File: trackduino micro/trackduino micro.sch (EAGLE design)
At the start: 28 parts, among them IC2 74AHC1G125DBV, SW1 SPST_TACT-KMR2, U1 ATMEGA168MLF, Y1 16MHZ

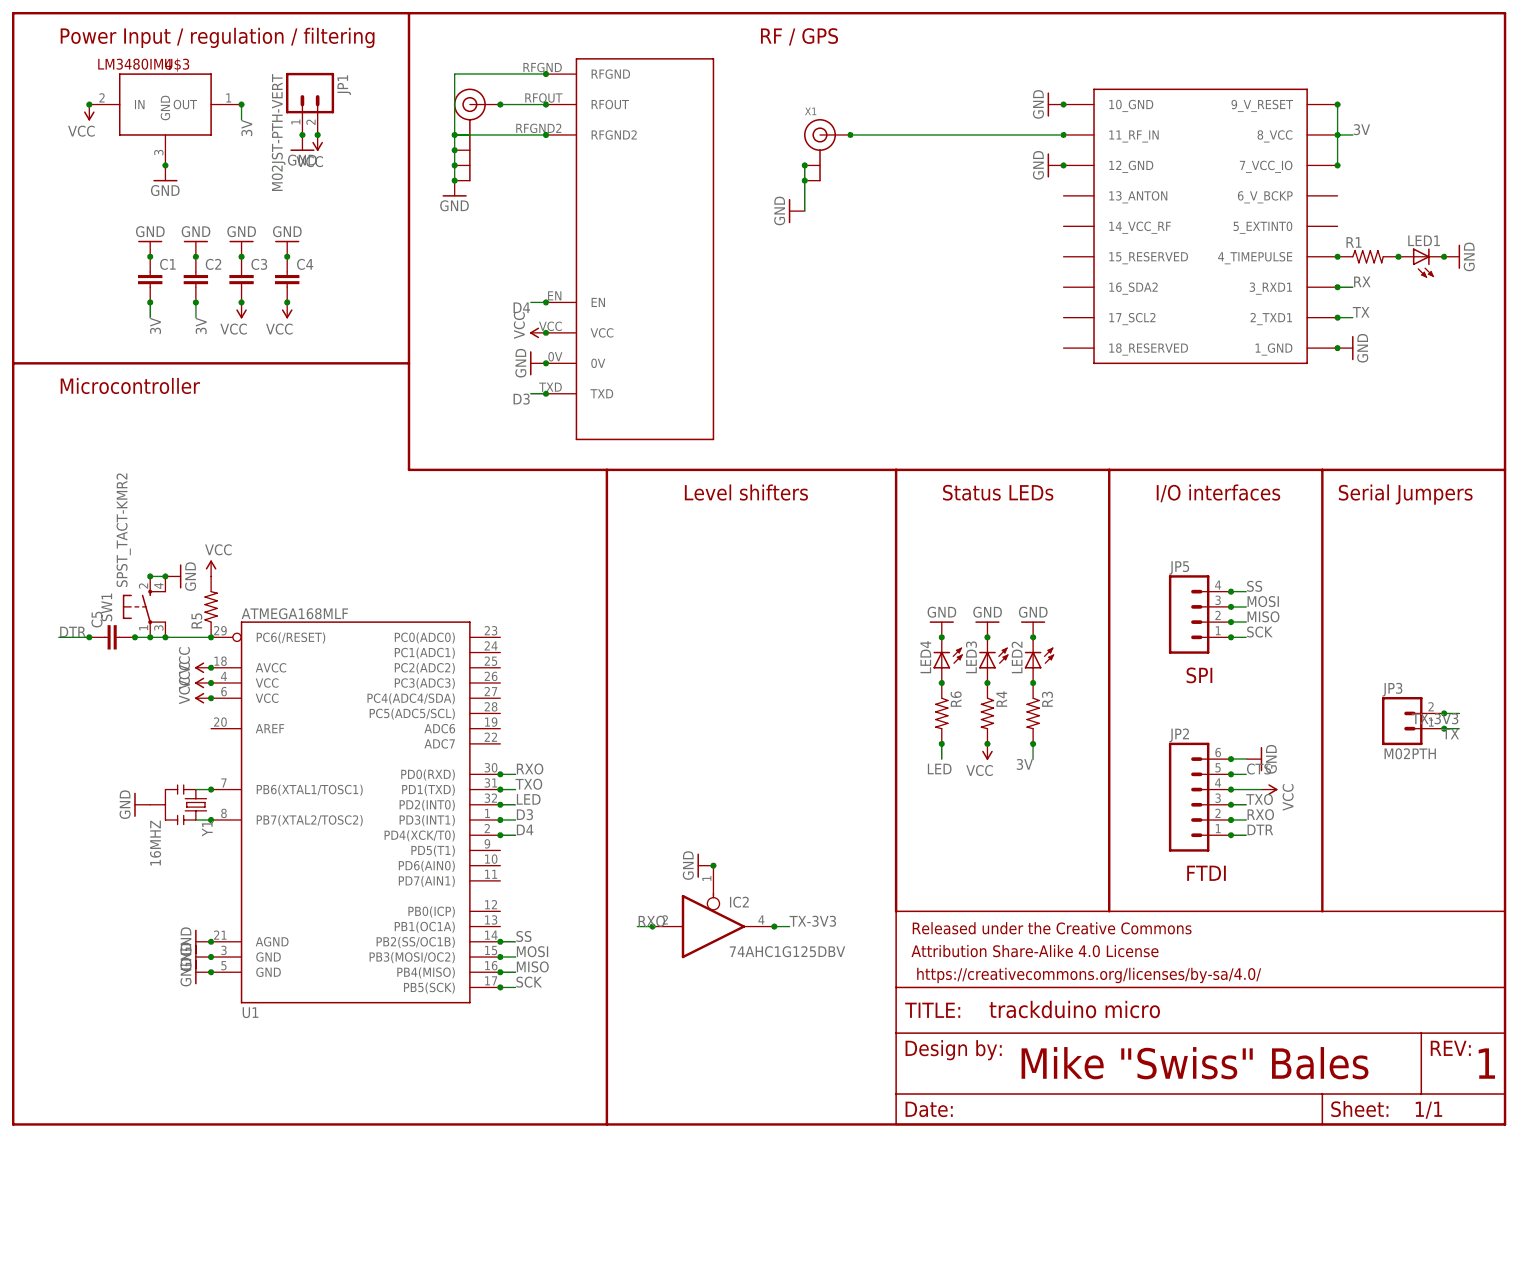
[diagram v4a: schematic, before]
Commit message: updated micro to mk1
to match the mini
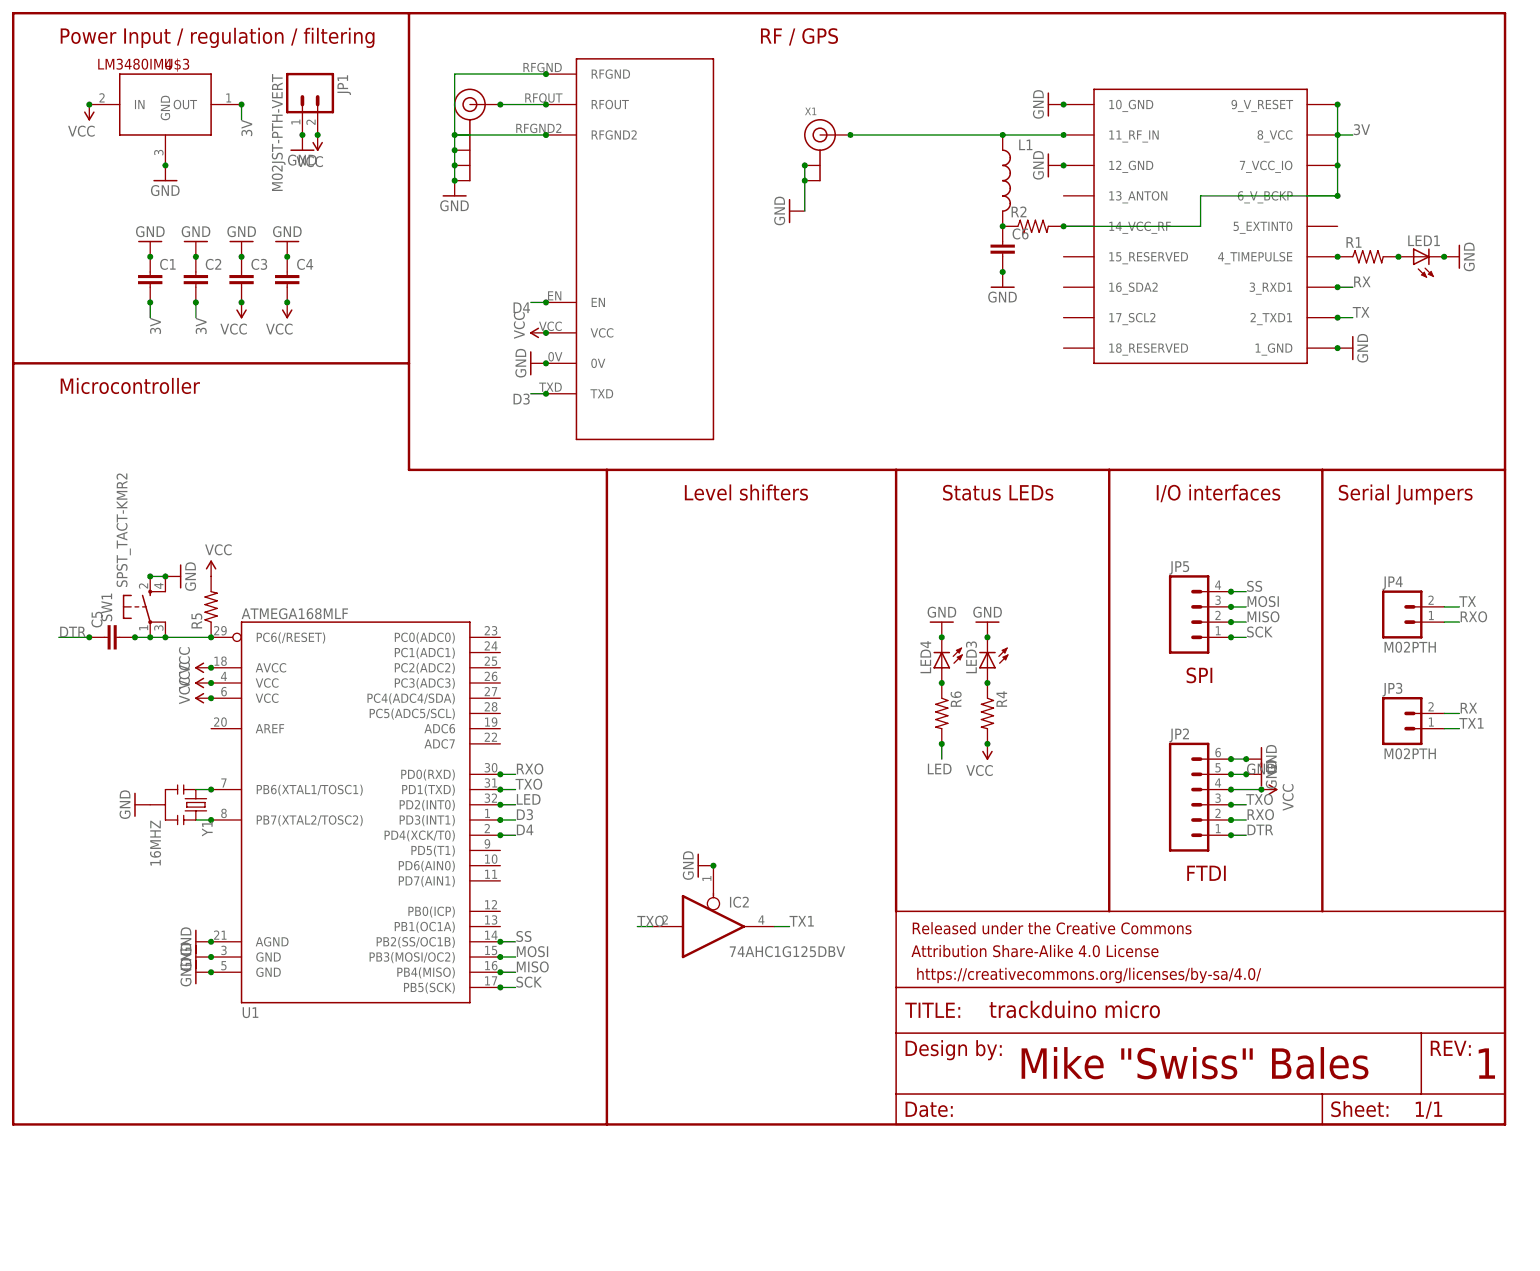
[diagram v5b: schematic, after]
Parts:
- removed LED2: (no value), adafruit:LEDCHIP-LED0805
- removed R3: (no value), SparkFun-Resistors:RESISTOR0805-RES
- added C6: (no value), SparkFun-Capacitors:CAP0805
- added JP4: M02PTH, SparkFun-Connectors:M02PTH
- added L1: (no value), SparkFun-Passives:INDUCTOR0805
- added R2: (no value), SparkFun-Resistors:RESISTOR0805-RES
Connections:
- removed net CTS: JP2.5
- removed net N$7: LED2.A, R3.1
- removed net TX-3V3: IC2A.O, JP3.2
- new net N$24: C6.1, L1.2, R2.1
- new net TX1: IC2A.O, JP3.1
- net 3V: now also R2.2, U$1.14_VCC_RF, U$1.6_V_BCKP; no longer R3.2
- net GND: now also C6.2, JP2.5; no longer LED2.C
- net N$6: now also L1.1
- net RX: now also JP3.2
- net RXO: now also JP4.1; no longer IC2A.I
- net TX: now also JP4.2; no longer JP3.1
- net TXO: now also IC2A.I
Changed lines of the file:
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@@
 <part name="SUPPLY4" library="SparkFun-Aesthetics" deviceset="VCC" device=""/>
 <part name="SUPPLY5" library="SparkFun-Aesthetics" deviceset="VCC" device=""/>
-<part name="LED2" library="adafruit" deviceset="LED" device="CHIP-LED0805"/>
-<part name="R3" library="SparkFun-Resistors" deviceset="RESISTOR" device="0805-RES"/>
 <part name="LED3" library="adafruit" deviceset="LED" device="CHIP-LED0805"/>
 <part name="R4" library="SparkFun-Resistors" deviceset="RESISTOR" device="0805-RES"/>
 <part name="GND19" library="SparkFun-Aesthetics" deviceset="GND" device=""/>
-<part name="GND20" library="SparkFun-Aesthetics" deviceset="GND" device=""/>
 <part name="SUPPLY6" library="SparkFun-Aesthetics" deviceset="VCC" device=""/>
 <part name="JP2" library="SparkFun-Connectors" deviceset="M06" device="NO_SILK_FEMALE_PTH"/>
@@
 <part name="GND1" library="SparkFun-Aesthetics" deviceset="GND" device=""/>
 <part name="GND3" library="SparkFun-Aesthetics" deviceset="GND" device=""/>
+<part name="L1" library="SparkFun-Passives" deviceset="INDUCTOR" device="0805"/>
+<part name="R2" library="SparkFun-Resistors" deviceset="RESISTOR" device="0805-RES"/>
+<part name="C6" library="SparkFun-Capacitors" deviceset="CAP" device="0805"/>
+<part name="GND6" library="SparkFun-Aesthetics" deviceset="GND" device=""/>
+<part name="JP4" library="SparkFun-Connectors" deviceset="M02" device="PTH"/>
+<part name="GND10" library="SparkFun-Aesthetics" deviceset="GND" device=""/>
 </parts>
 <sheets>
@@
 <instance part="SUPPLY4" gate="G$1" x="38.1" y="137.16" rot="R180"/>
 <instance part="SUPPLY5" gate="G$1" x="45.72" y="137.16" rot="R180"/>
-<instance part="LED2" gate="G$1" x="170.18" y="76.2" rot="R180"/>
-<instance part="R3" gate="G$1" x="170.18" y="68.58" rot="R270"/>
 <instance part="LED3" gate="G$1" x="162.56" y="76.2" rot="R180"/>
 <instance part="R4" gate="G$1" x="162.56" y="68.58" rot="R270"/>
 <instance part="GND19" gate="1" x="162.56" y="83.82" rot="R180"/>
-<instance part="GND20" gate="1" x="170.18" y="83.82" rot="R180"/>
 <instance part="SUPPLY6" gate="G$1" x="162.56" y="63.5" rot="R180"/>
 <instance part="JP2" gate="G$1" x="198.12" y="53.34"/>
@@
 <instance part="GND1" gate="1" x="30.48" y="147.32" rot="R180"/>
 <instance part="GND3" gate="1" x="25.4" y="157.48"/>
+<instance part="L1" gate="G$1" x="165.1" y="157.48"/>
+<instance part="R2" gate="G$1" x="170.18" y="149.86"/>
+<instance part="C6" gate="G$1" x="165.1" y="144.78"/>
+<instance part="GND6" gate="1" x="165.1" y="139.7"/>
+<instance part="JP4" gate="G$1" x="231.14" y="83.82"/>
+<instance part="GND10" gate="1" x="208.28" y="58.42" rot="R90"/>
 </instances>
 <busses>
@@
 </segment>
 <segment>
-<pinref part="LED2" gate="G$1" pin="C"/>
-<pinref part="GND20" gate="1" pin="GND"/>
-<junction x="170.18" y="81.28"/>
-</segment>
-<segment>
 <pinref part="LED3" gate="G$1" pin="C"/>
 <pinref part="GND19" gate="1" pin="GND"/>
@@
 <pinref part="GND22" gate="1" pin="GND"/>
 <junction x="203.2" y="60.96"/>
+<junction x="205.74" y="60.96"/>
 </segment>
 <segment>
@@
 <junction x="25.4" y="160.02"/>
 </segment>
-</net>
-<net name="TX-3V3" class="0">
-<segment>
-<pinref part="IC2" gate="A" pin="O"/>
-<wire x1="127" y1="33.02" x2="129.54" y2="33.02" width="0.1524" layer="91"/>
-<label x="129.54" y="33.02" size="1.778" layer="95"/>
-<junction x="127" y="33.02"/>
-</segment>
-<segment>
-<pinref part="JP3" gate="G$1" pin="2"/>
-<wire x1="238.76" y1="68.58" x2="241.3" y2="68.58" width="0.1524" layer="91"/>
-<label x="241.3" y="68.58" size="1.778" layer="95" rot="R180"/>
-<junction x="238.76" y="68.58"/>
+<segment>
+<pinref part="C6" gate="G$1" pin="2"/>
+<pinref part="GND6" gate="1" pin="GND"/>
+<junction x="165.1" y="142.24"/>
+</segment>
+<segment>
+<pinref part="JP2" gate="G$1" pin="5"/>
+<wire x1="203.2" y1="58.42" x2="205.74" y2="58.42" width="0.1524" layer="91"/>
+<label x="205.74" y="58.42" size="1.778" layer="95"/>
+<junction x="203.2" y="58.42"/>
+<pinref part="GND10" gate="1" pin="GND"/>
+<junction x="205.74" y="58.42"/>
 </segment>
 </net>
@@
 <net name="TX" class="0">
 <segment>
-<pinref part="JP3" gate="G$1" pin="1"/>
-<wire x1="238.76" y1="66.04" x2="241.3" y2="66.04" width="0.1524" layer="91"/>
-<label x="241.3" y="66.04" size="1.778" layer="95" rot="R180"/>
-<junction x="238.76" y="66.04"/>
-</segment>
-<segment>
 <wire x1="220.98" y1="134.62" x2="223.52" y2="134.62" width="0.1524" layer="91"/>
 <label x="223.52" y="134.62" size="1.778" layer="95"/>
@@
 <junction x="220.98" y="134.62"/>
 </segment>
+<segment>
+<pinref part="JP4" gate="G$1" pin="2"/>
+<wire x1="238.76" y1="86.36" x2="241.3" y2="86.36" width="0.1524" layer="91"/>
+<label x="241.3" y="86.36" size="1.778" layer="95"/>
+</segment>
 </net>
 <net name="D4" class="0">
@@
 <pinref part="SUPPLY9" gate="G$1" pin="VCC"/>
 <junction x="203.2" y="55.88"/>
+<junction x="208.28" y="55.88"/>
 </segment>
 <segment>
@@
 <wire x1="220.98" y1="165.1" x2="220.98" y2="160.02" width="0.1524" layer="91"/>
 <junction x="220.98" y="170.18"/>
+<pinref part="U$1" gate="G$1" pin="6_V_BCKP"/>
+<wire x1="220.98" y1="160.02" x2="220.98" y2="154.94" width="0.1524" layer="91"/>
+<wire x1="220.98" y1="154.94" x2="198.12" y2="154.94" width="0.1524" layer="91"/>
+<wire x1="198.12" y1="154.94" x2="198.12" y2="149.86" width="0.1524" layer="91"/>
+<pinref part="U$1" gate="G$1" pin="14_VCC_RF"/>
+<wire x1="198.12" y1="149.86" x2="175.26" y2="149.86" width="0.1524" layer="91"/>
+<pinref part="R2" gate="G$1" pin="2"/>
+<junction x="175.26" y="149.86"/>
+<junction x="220.98" y="154.94"/>
 </segment>
 <segment>
@@
 <label x="22.86" y="134.62" size="1.778" layer="95" rot="R270"/>
 <junction x="22.86" y="137.16"/>
-</segment>
-<segment>
-<pinref part="R3" gate="G$1" pin="2"/>
-<wire x1="170.18" y1="63.5" x2="170.18" y2="60.96" width="0.1524" layer="91"/>
-<label x="170.18" y="60.96" size="1.778" layer="95" rot="R180"/>
-<junction x="170.18" y="63.5"/>
 </segment>
 </net>
@@
 <net name="N$6" class="0">
 <segment>
-<wire x1="175.26" y1="165.1" x2="139.7" y2="165.1" width="0.1524" layer="91"/>
+<wire x1="175.26" y1="165.1" x2="165.1" y2="165.1" width="0.1524" layer="91"/>
 <pinref part="U$1" gate="G$1" pin="11_RF_IN"/>
 <pinref part="X1" gate="G$1" pin="SIGNAL"/>
 <junction x="139.7" y="165.1"/>
 <junction x="175.26" y="165.1"/>
+<pinref part="L1" gate="G$1" pin="1"/>
+<wire x1="165.1" y1="165.1" x2="139.7" y2="165.1" width="0.1524" layer="91"/>
+<junction x="165.1" y="165.1"/>
 </segment>
 </net>
@@
 <junction x="220.98" y="139.7"/>
 </segment>
-</net>
-<net name="N$7" class="0">
-<segment>
-<pinref part="R3" gate="G$1" pin="1"/>
-<pinref part="LED2" gate="G$1" pin="A"/>
-<junction x="170.18" y="73.66"/>
+<segment>
+<pinref part="JP3" gate="G$1" pin="2"/>
+<wire x1="238.76" y1="68.58" x2="241.3" y2="68.58" width="0.1524" layer="91"/>
+<label x="241.3" y="68.58" size="1.778" layer="95"/>
 </segment>
 </net>
@@
 <pinref part="R4" gate="G$1" pin="1"/>
 <junction x="162.56" y="73.66"/>
-</segment>
-</net>
-<net name="CTS" class="0">
-<segment>
-<pinref part="JP2" gate="G$1" pin="5"/>
-<wire x1="203.2" y1="58.42" x2="205.74" y2="58.42" width="0.1524" layer="91"/>
-<label x="205.74" y="58.42" size="1.778" layer="95"/>
-<junction x="203.2" y="58.42"/>
 </segment>
 </net>
@@
 </segment>
 <segment>
-<pinref part="IC2" gate="A" pin="I"/>
-<wire x1="106.68" y1="33.02" x2="104.14" y2="33.02" width="0.1524" layer="91"/>
-<label x="104.14" y="33.02" size="1.778" layer="95"/>
-<junction x="106.68" y="33.02"/>
+<pinref part="JP4" gate="G$1" pin="1"/>
+<wire x1="238.76" y1="83.82" x2="241.3" y2="83.82" width="0.1524" layer="91"/>
+<label x="241.3" y="83.82" size="1.778" layer="95"/>
 </segment>
 </net>
@@
 <junction x="203.2" y="53.34"/>
 </segment>
+<segment>
+<pinref part="IC2" gate="A" pin="I"/>
+<wire x1="106.68" y1="33.02" x2="104.14" y2="33.02" width="0.1524" layer="91"/>
+<label x="104.14" y="33.02" size="1.778" layer="95"/>
+</segment>
 </net>
 <net name="MISO" class="0">
@@
 </segment>
 </net>
+<net name="N$24" class="0">
+<segment>
+<pinref part="R2" gate="G$1" pin="1"/>
+<pinref part="L1" gate="G$1" pin="2"/>
+<pinref part="C6" gate="G$1" pin="1"/>
+<junction x="165.1" y="149.86"/>
+<pinref part="C6" gate="G$1" pin="1"/>
+</segment>
+</net>
+<net name="TX1" class="0">
+<segment>
+<pinref part="IC2" gate="A" pin="O"/>
+<wire x1="127" y1="33.02" x2="129.54" y2="33.02" width="0.1524" layer="91"/>
+<label x="129.54" y="33.02" size="1.778" layer="95"/>
+</segment>
+<segment>
+<pinref part="JP3" gate="G$1" pin="1"/>
+<wire x1="238.76" y1="66.04" x2="241.3" y2="66.04" width="0.1524" layer="91"/>
+<label x="241.3" y="66.04" size="1.778" layer="95"/>
+</segment>
+</net>
